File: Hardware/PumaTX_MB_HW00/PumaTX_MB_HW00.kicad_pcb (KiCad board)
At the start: 4 copper layers, 130 x 40 mm, 106 parts, among them J100 FH12A-26S-0.5SH_55_, J101 FH12-12S-0.5SH_55_, J102 500334-0160, J103 500334-0160, J104 692122030100, J105 53398-0667, J300 U.FL-R-SMT-1_40_, J410 U.FL-R-SMT-1_40_, M130 Motor_DC, M140 Fan, Q130 ZXMN3B01F, Q140 ZXMN3B01F, Q200 UMH3NTN, Q201 UMH3NTN, U200 CP2105-F01-GMR, U300 ESP32-PICO-D4, U400 ESP32-PICO-D4, U402 E28-2G4M27S, U410 SX1280, U500 BQ24075RGTR, U510 MIC5528-3.3YMT-T5, U520 MIC5528-3.3YMT-T5, U530 MIC5528-3.3YMT-T5, Y410 NX2016SA-52MHZ-EXS00A-CS06016

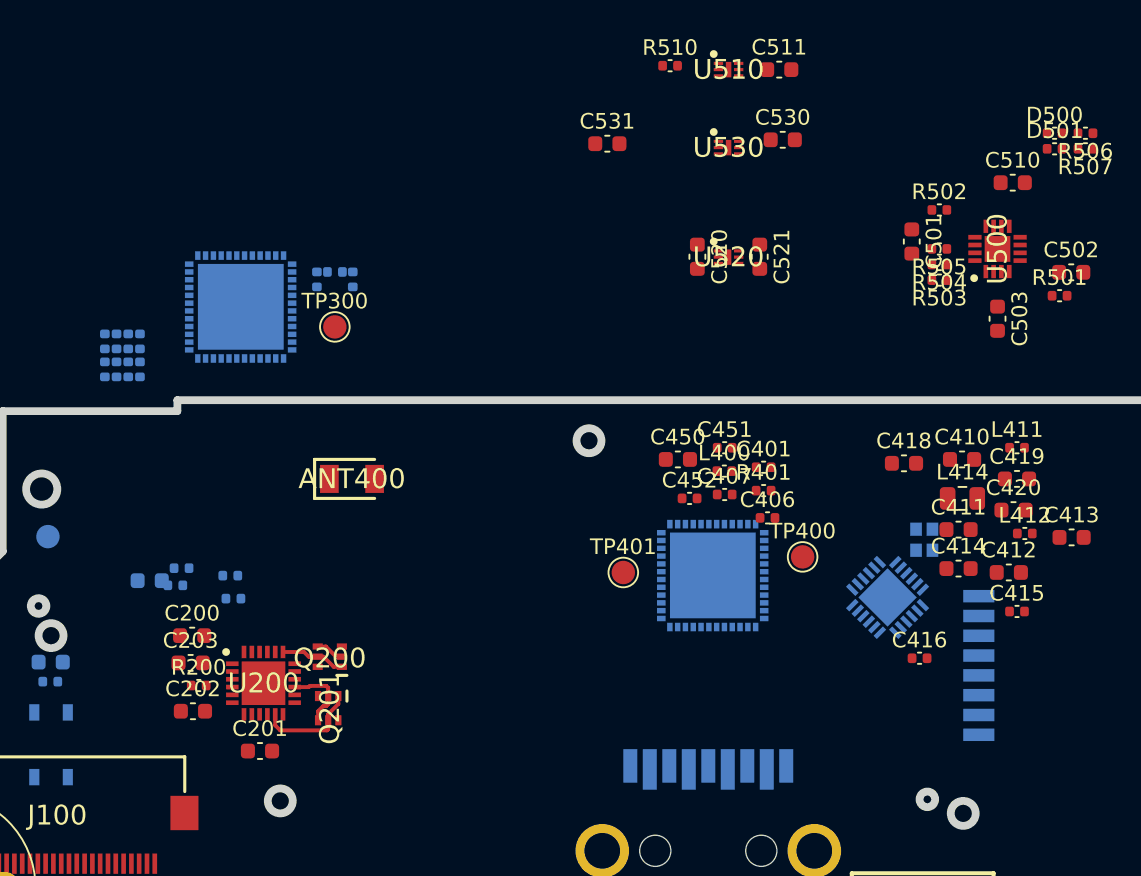
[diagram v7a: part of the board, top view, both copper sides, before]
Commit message: updated layout
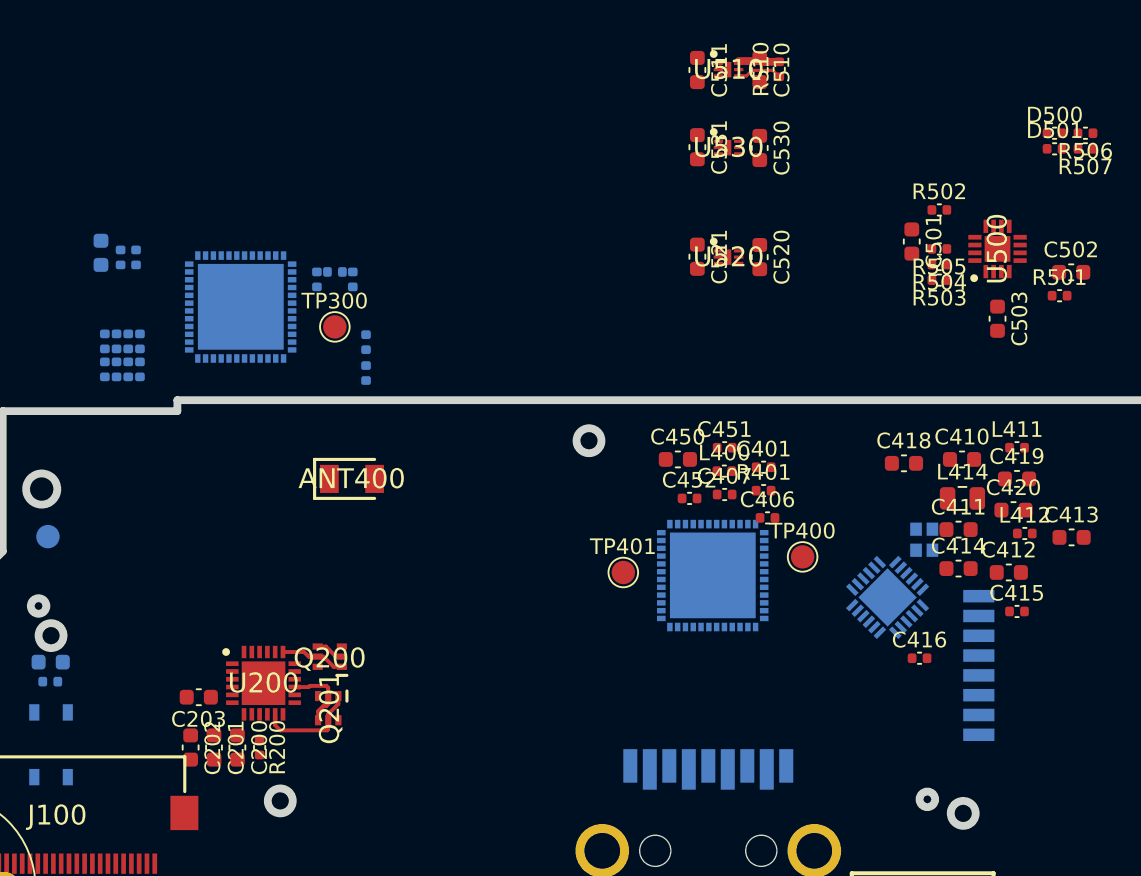
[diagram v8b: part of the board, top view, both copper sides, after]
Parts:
- moved C351 21.3 mm to (108.3, 74.0), turned to -90 degrees
- moved C350 21.3 mm to (107.0, 73.8), turned to -90 degrees
- moved C352 20.1 mm to (109.2, 74.0), turned to -90 degrees
- moved C510 17.8 mm to (149.2, 62.0), turned to -90 degrees
- moved R300 17.3 mm to (124.0, 79.5), turned to -90 degrees
- moved C300 16.8 mm to (124.0, 81.5), turned to -90 degrees
- moved C200 7.74 mm to (115.8, 105.5), turned to -90 degrees
- moved R510 7.00 mm to (150.5, 62.0), turned to 90 degrees
- moved C531 5.78 mm to (145.2, 67.0), turned to -90 degrees
- moved R200 5.57 mm to (117.2, 105.5), turned to -90 degrees
- moved C511 5.25 mm to (145.2, 62.0), turned to -90 degrees
- moved C520 4.00 mm to (149.2, 74.0)
- moved C521 4.00 mm to (145.2, 74.0)
- moved C201 2.96 mm to (114.2, 105.5), turned to -90 degrees
- moved C202 2.33 mm to (112.8, 105.5), turned to -90 degrees
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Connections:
- C520 pad 1: Net-(C520-Pad1) -> /VSYS
- C530 pad 1: Net-(C530-Pad1) -> /VSYS
- U520 pad 6: Net-(C520-Pad1) -> /VSYS
- U530 pad 6: Net-(C530-Pad1) -> /VSYS
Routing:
- net /3V3_EN: track 0.00 -> 2.91 mm
- net /VSYS: track 0.00 -> 2.79 mm
